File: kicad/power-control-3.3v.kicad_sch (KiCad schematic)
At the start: 16 parts, among them J5 USB_C_Receptacle_USB2.0, U1 MCP73871, U10 MCP1700x-180xxTT, U11 USBLC6-2P6

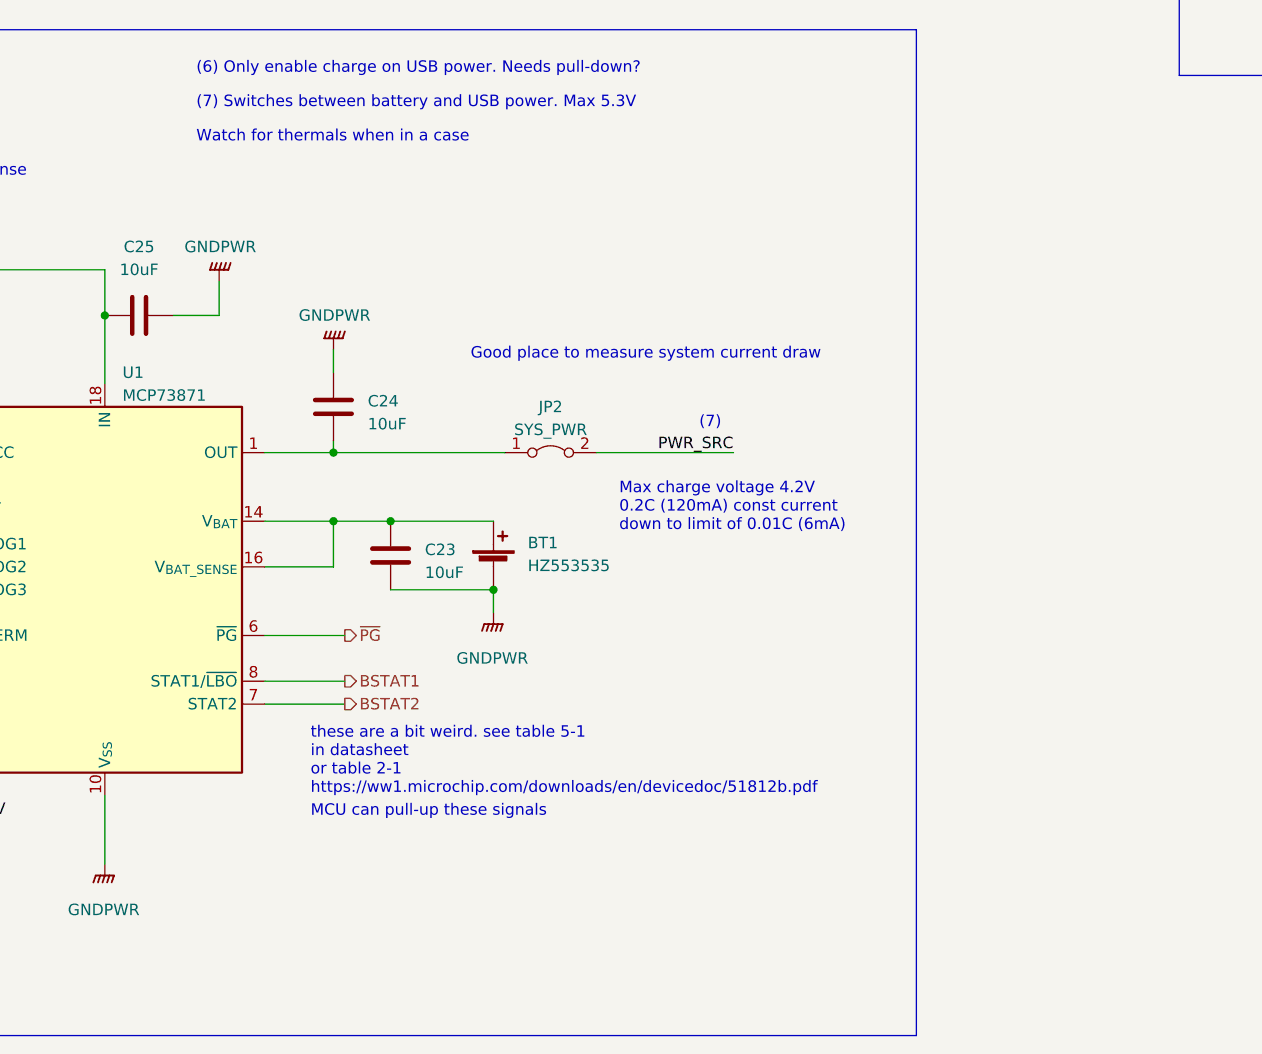
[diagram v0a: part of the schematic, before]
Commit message: hw: update power symbols, clean up some power circuitry
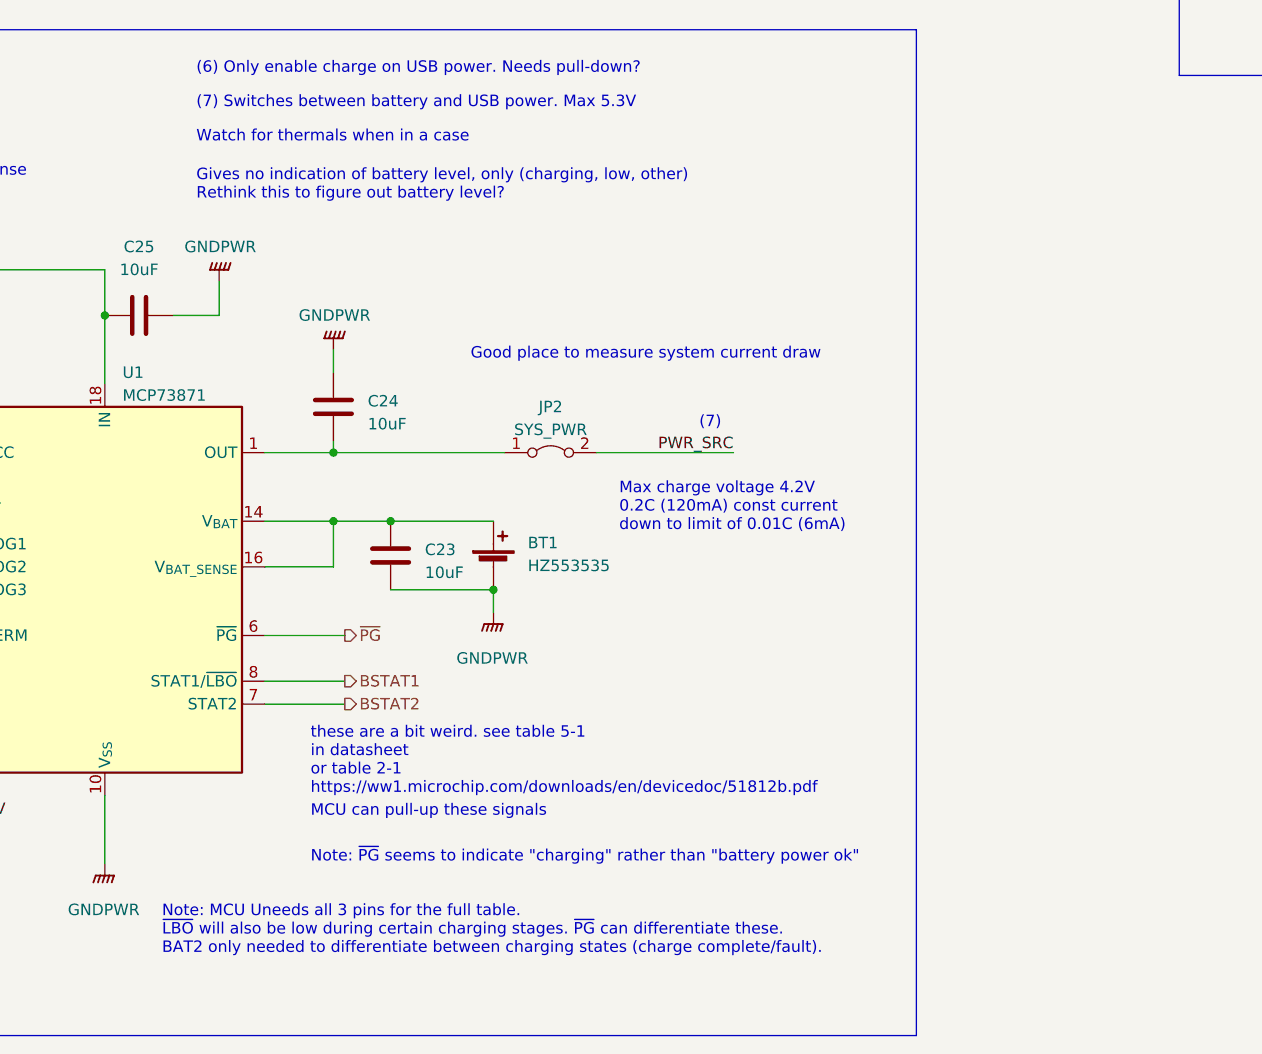
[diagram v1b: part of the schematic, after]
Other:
- note added: "Gives no indication of battery level, only (charging, low, other) Rethink this to figure out battery level?"
- note added: "Note: MCU Uneeds all 3 pins for the full table. ~{LBO} will also be low during certain charging stages. ~{PG} can differentiate these. BAT2 only needed to differentiate between charging states (charge complete/fault)."
- note added: "Note: ~{PG} seems to indicate "charging" rather than "battery power ok""
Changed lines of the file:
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@@
+    (effects (font (size 1.27 1.27)) (justify left bottom))
+  )
+  (text "Note: ~{PG} seems to indicate \"charging\" rather than \"battery power ok\""
+    (at 101.6 173.99 0)
     (effects (font (size 1.27 1.27)) (justify left bottom))
   )
@@
     (effects (font (size 1.27 1.27)) (justify left bottom))
   )
+  (text "Gives no indication of battery level, only (charging, low, other)\nRethink this to figure out battery level?"
+    (at 88.9 100.33 0)
+    (effects (font (size 1.27 1.27)) (justify left bottom))
+  )
   (text "(7)" (at 144.78 125.73 0)
     (effects (font (size 1.27 1.27)) (justify left bottom))
@@
     (effects (font (size 1.27 1.27)) (justify left bottom))
   )
+  (text "Note: MCU Uneeds all 3 pins for the full table.\n~{LBO} will also be low during certain charging stages. ~{PG} can differentiate these.\nBAT2 only needed to differentiate between charging states (charge complete/fault)."
+    (at 85.09 184.15 0)
+    (effects (font (size 1.27 1.27)) (justify left bottom))
+  )

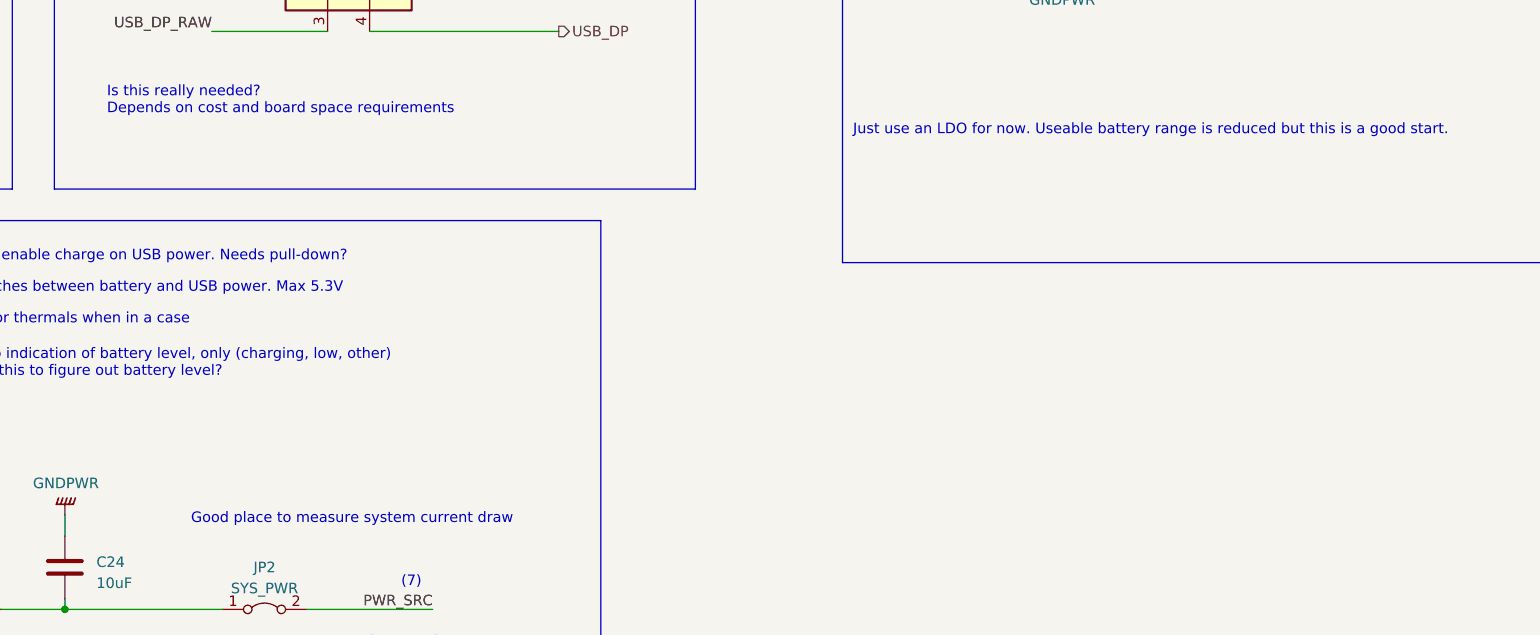
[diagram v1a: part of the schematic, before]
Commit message: hw: more consideration on battery circuit
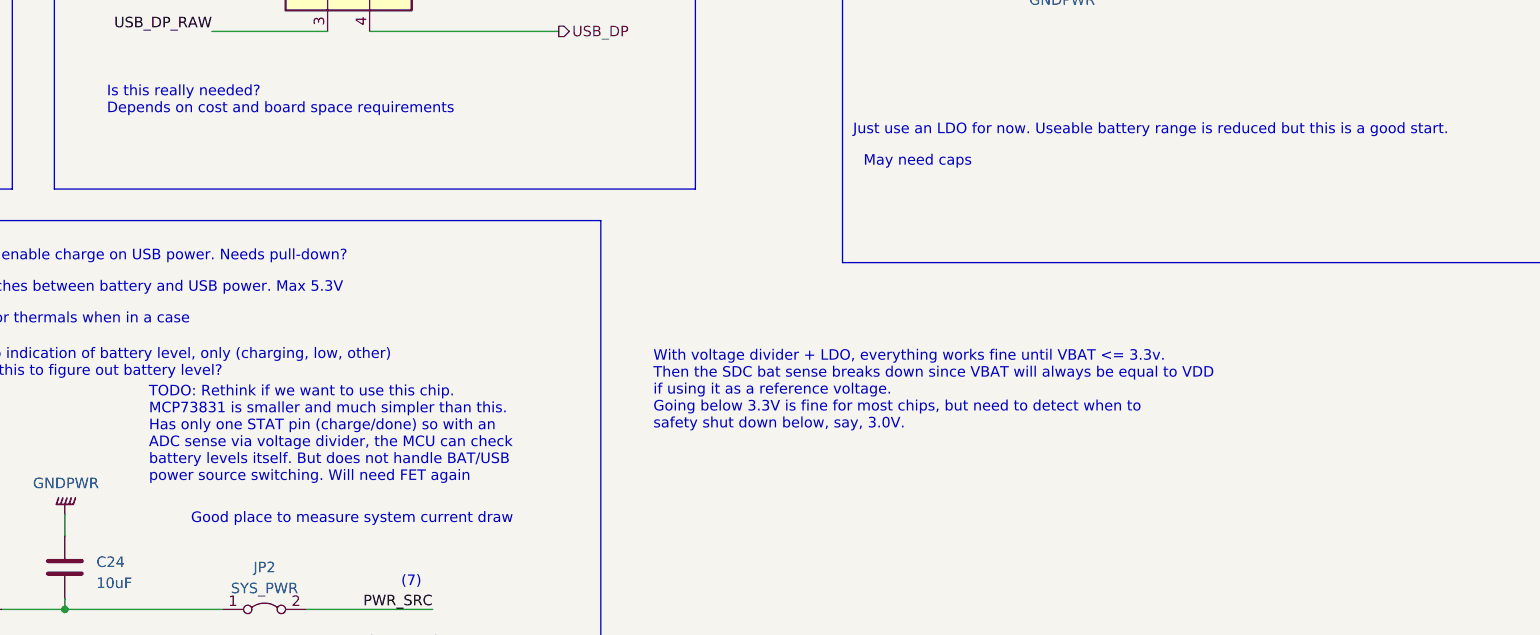
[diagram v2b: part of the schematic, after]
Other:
- note added: "May need caps"
- note added: "TODO: Rethink if we want to use this chip. MCP73831 is smaller and much simpler than this. Has only one STAT pin (charge/done) so with an ADC sense via voltage divider, the MCU can check battery levels itself. But does not handle BAT/USB power source switching. Will need FET again"
- note added: "With voltage divider + LDO, everything works fine until VBAT <= 3.3v. Then the SDC bat sense breaks down since VBAT will always be equal to VDD if using it as a reference voltage. Going below 3.3V is fine for most chips, but need to detect when to safety shut down below, say, 3.0V."
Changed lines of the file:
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@@
+    (effects (font (size 1.27 1.27)) (justify left bottom))
+  )
+  (text "May need caps" (at 200.66 74.93 0)
     (effects (font (size 1.27 1.27)) (justify left bottom))
   )
@@
   (text "Watch for thermals when in a case" (at 88.9 93.98 0)
     (effects (font (size 1.27 1.27) (color 255 1 18 1)) (justify left bottom))
+  )
+  (text "TODO: Rethink if we want to use this chip.\nMCP73831 is smaller and much simpler than this.\nHas only one STAT pin (charge/done) so with an\nADC sense via voltage divider, the MCU can check \nbattery levels itself. But does not handle BAT/USB\npower source switching. Will need FET again\n"
+    (at 114.3 113.03 0)
+    (effects (font (size 1.27 1.27)) (justify left bottom))
   )
   (text "Max charge voltage 4.2V\n0.2C (120mA) const current \ndown to limit of 0.01C (6mA)"
@@
     (effects (font (size 1.27 1.27)) (justify left bottom))
   )
+  (text "With voltage divider + LDO, everything works fine until VBAT <= 3.3v.\nThen the SDC bat sense breaks down since VBAT will always be equal to VDD \nif using it as a reference voltage.\nGoing below 3.3V is fine for most chips, but need to detect when to \nsafety shut down below, say, 3.0V."
+    (at 175.26 106.68 0)
+    (effects (font (size 1.27 1.27)) (justify left bottom))
+  )
